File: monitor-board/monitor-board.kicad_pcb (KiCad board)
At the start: 2 copper layers, 55.9 x 53.3 mm, 26 parts, among them SW1 SW_IO12, SW2 SW_IO13, SW3 SW_IO14, SW4 SW_IO15, SW5 SW_IO32, SW6 SW_IO33, SW7 SW_IO34, SW8 SW_IO35, U1 ESP32-WROOM-32, U2 TLV75533PDBV

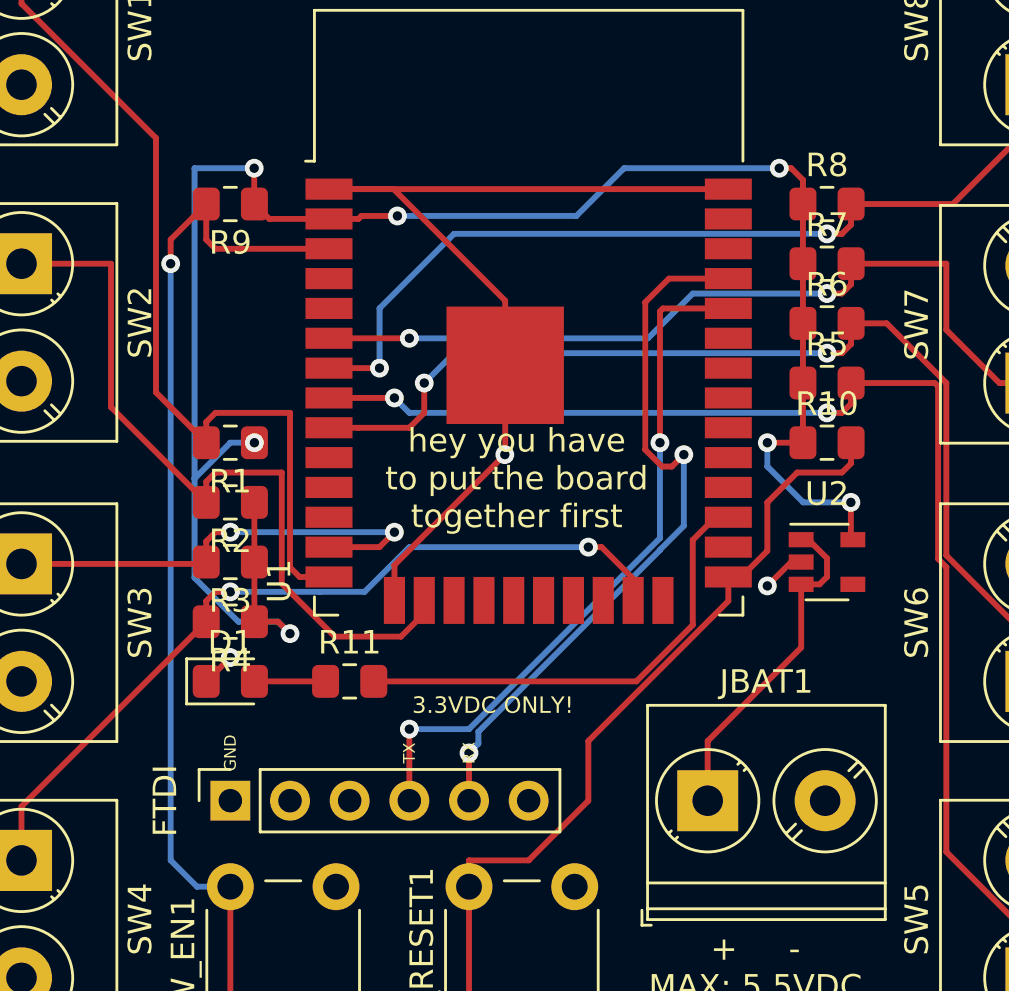
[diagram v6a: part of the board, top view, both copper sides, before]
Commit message: Update footprints of resistors and led to go with cheap parts
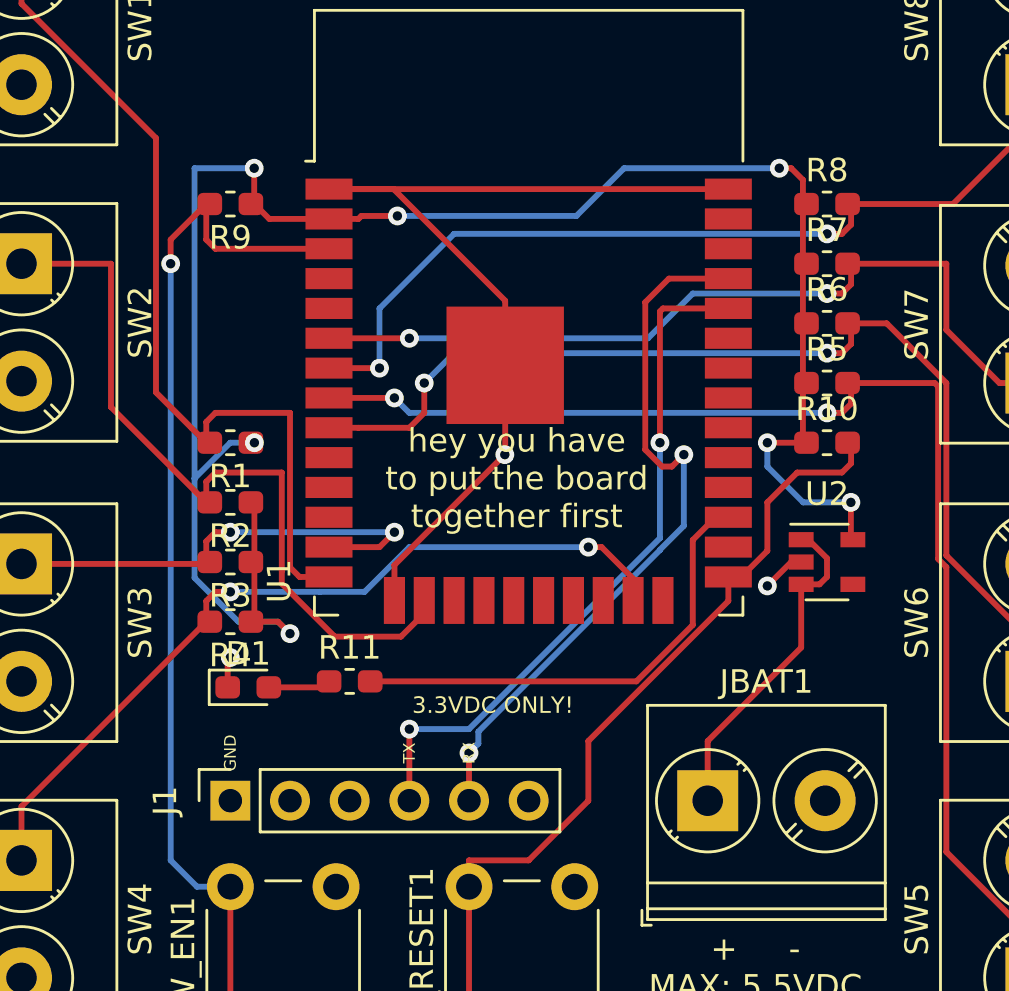
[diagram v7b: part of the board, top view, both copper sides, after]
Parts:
- D1: footprint LED_SMD:LED_0805_2012Metric_Pad1.15x1.40mm_HandSolder -> LED_SMD:LED_0603_1608Metric_Pad1.05x0.95mm_HandSolder
- R1, R10, R11, R2, R3, R4, R5, R6, R7, R8, R9: footprint Resistor_SMD:R_0805_2012Metric_Pad1.15x1.40mm_HandSolder -> Resistor_SMD:R_0603_1608Metric_Pad1.05x0.95mm_HandSolder
- moved D1 0.80 mm to (41.4, 61.2)
- renumbered FTDI to J1
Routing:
- net Net-(D1-Pad2): track 3.03 -> 2.52 mm

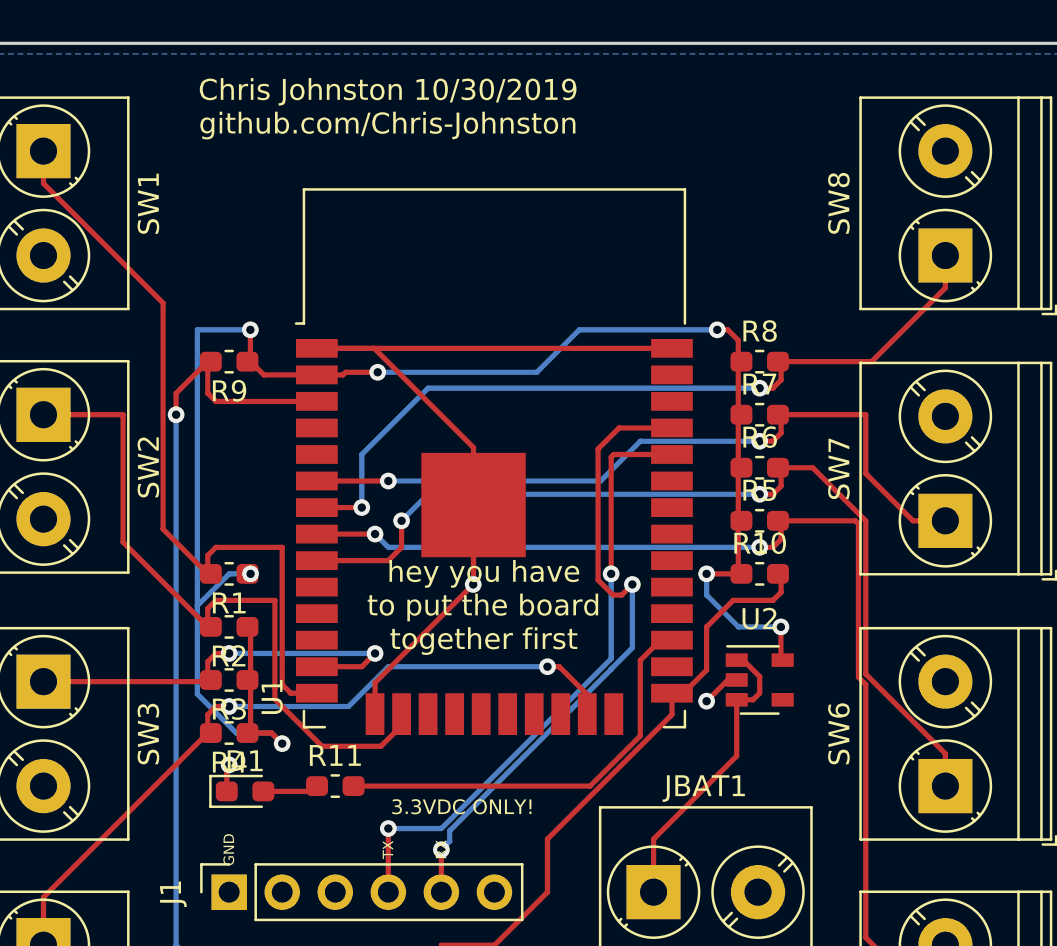
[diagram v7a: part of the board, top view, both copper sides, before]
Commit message: dont add crob image
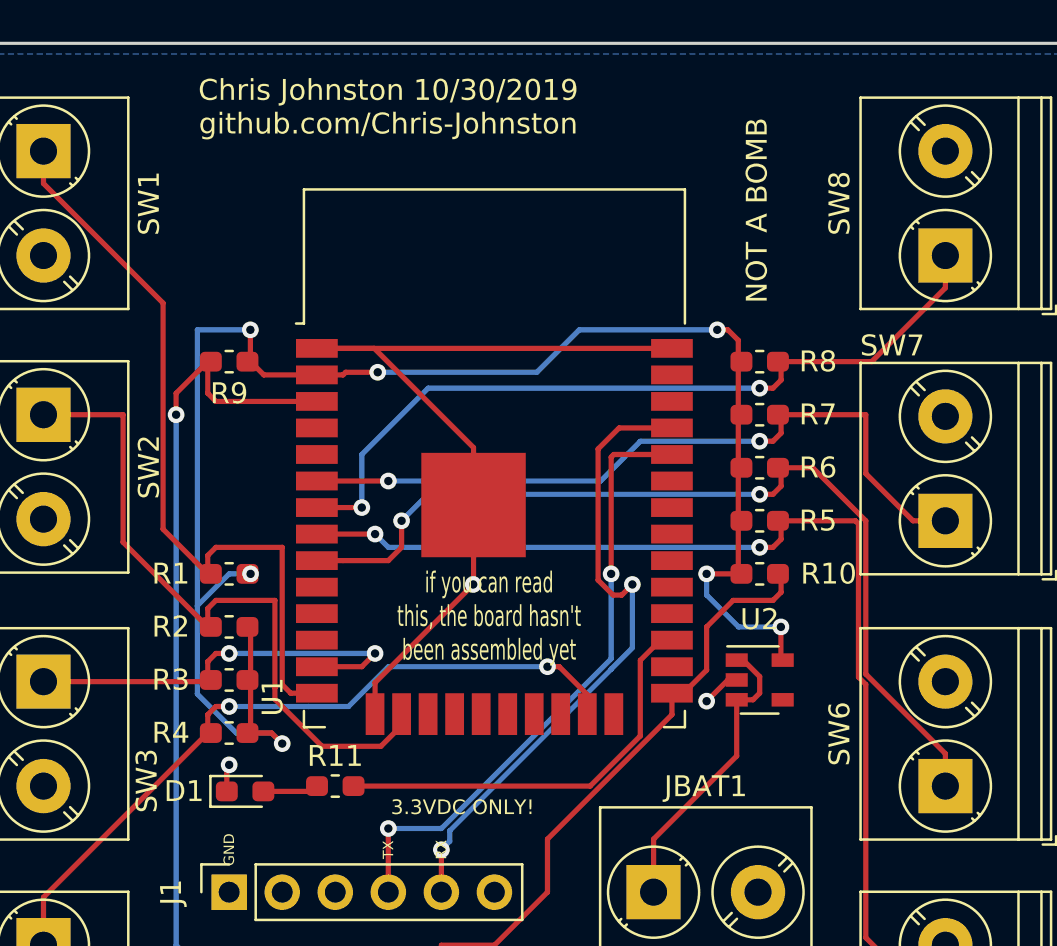
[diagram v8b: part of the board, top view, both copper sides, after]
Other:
- board text added: "FRONT TOWARD ENEMY"
- board text added: "NOT A BOMB"
- board text added: "if you can read this, the board hasn't been assembled yet"
- board text removed: "hey you have to put the board together first"
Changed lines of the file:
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@@
   (general
     (thickness 1.6)
-    (drawings 12)
+    (drawings 14)
     (tracks 225)
     (zones 0)
@@
   (page A4)
   (layers
-    (0 F.Cu signal)
-    (31 B.Cu signal)
-    (33 F.Adhes user)
-    (35 F.Paste user)
+    (0 F.Cu signal hide)
+    (31 B.Cu signal hide)
+    (33 F.Adhes user hide)
+    (35 F.Paste user hide)
+    (36 B.SilkS user)
     (37 F.SilkS user)
     (39 F.Mask user)
-    (40 Dwgs.User user)
-    (41 Cmts.User user)
-    (42 Eco1.User user)
-    (43 Eco2.User user)
+    (40 Dwgs.User user hide)
+    (41 Cmts.User user hide)
+    (42 Eco1.User user hide)
+    (43 Eco2.User user hide)
     (44 Edge.Cuts user)
-    (45 Margin user)
-    (46 B.CrtYd user)
-    (47 F.CrtYd user)
-    (49 F.Fab user)
+    (45 Margin user hide)
+    (46 B.CrtYd user hide)
+    (47 F.CrtYd user hide)
+    (49 F.Fab user hide)
   )
   (setup
@@
     (descr "Terminal Block Phoenix PT-1,5-2-5.0-H, 2 pins, pitch 5mm, size 10x9mm^2, drill diamater 1.3mm, pad diameter 2.6mm, see http://www.mouser.com/ds/2/324/ItemDetail_1935161-922578.pdf, script-generated using https://github.com/pointhi/kicad-footprint-generator/scripts/TerminalBlock_Phoenix")
     (tags "THT Terminal Block Phoenix PT-1,5-2-5.0-H pitch 5mm size 10x9mm^2 drill 1.3mm pad 2.6mm")
-    (fp_text reference SW3 (at 2.5 -5.06 90) (layer F.SilkS)
+    (fp_text reference SW3 (at 4.746 -4.953 90) (layer F.SilkS)
       (effects (font (size 1 1) (thickness 0.15)))
     )
@@
     (descr "Terminal Block Phoenix PT-1,5-2-5.0-H, 2 pins, pitch 5mm, size 10x9mm^2, drill diamater 1.3mm, pad diameter 2.6mm, see http://www.mouser.com/ds/2/324/ItemDetail_1935161-922578.pdf, script-generated using https://github.com/pointhi/kicad-footprint-generator/scripts/TerminalBlock_Phoenix")
     (tags "THT Terminal Block Phoenix PT-1,5-2-5.0-H pitch 5mm size 10x9mm^2 drill 1.3mm pad 2.6mm")
-    (fp_text reference SW7 (at 2.5 -5.06 90) (layer F.SilkS)
+    (fp_text reference SW7 (at 8.382 -2.54 180) (layer F.SilkS)
       (effects (font (size 1 1) (thickness 0.15)))
     )
@@
     (tags "LED handsolder")
     (attr smd)
-    (fp_text reference D1 (at 0 -1.43) (layer F.SilkS)
+    (fp_text reference D1 (at -2.921 0) (layer F.SilkS)
       (effects (font (size 1 1) (thickness 0.15)))
     )
@@
     (tags "resistor handsolder")
     (attr smd)
-    (fp_text reference R1 (at 0 -1.43) (layer F.SilkS)
+    (fp_text reference R1 (at 2.794 0) (layer F.SilkS)
       (effects (font (size 1 1) (thickness 0.15)))
     )
@@
     (tags "resistor handsolder")
     (attr smd)
-    (fp_text reference R2 (at 0 -1.43) (layer F.SilkS)
+    (fp_text reference R2 (at 2.794 0) (layer F.SilkS)
       (effects (font (size 1 1) (thickness 0.15)))
     )
@@
     (tags "resistor handsolder")
     (attr smd)
-    (fp_text reference R3 (at 0 -1.43) (layer F.SilkS)
+    (fp_text reference R3 (at 2.794 0) (layer F.SilkS)
       (effects (font (size 1 1) (thickness 0.15)))
     )
@@
     (tags "resistor handsolder")
     (attr smd)
-    (fp_text reference R4 (at 0 -1.43) (layer F.SilkS)
+    (fp_text reference R4 (at 2.794 0) (layer F.SilkS)
       (effects (font (size 1 1) (thickness 0.15)))
     )
@@
     (tags "resistor handsolder")
     (attr smd)
-    (fp_text reference R5 (at 0 -1.43) (layer F.SilkS)
+    (fp_text reference R5 (at 2.794 0) (layer F.SilkS)
       (effects (font (size 1 1) (thickness 0.15)))
     )
@@
     (tags "resistor handsolder")
     (attr smd)
-    (fp_text reference R6 (at 0 -1.43) (layer F.SilkS)
+    (fp_text reference R6 (at 2.794 0) (layer F.SilkS)
       (effects (font (size 1 1) (thickness 0.15)))
     )
@@
     (tags "resistor handsolder")
     (attr smd)
-    (fp_text reference R7 (at 0 -1.43) (layer F.SilkS)
+    (fp_text reference R7 (at 2.794 0) (layer F.SilkS)
       (effects (font (size 1 1) (thickness 0.15)))
     )
@@
     (tags "resistor handsolder")
     (attr smd)
-    (fp_text reference R8 (at 0 -1.43) (layer F.SilkS)
+    (fp_text reference R8 (at 2.794 0) (layer F.SilkS)
       (effects (font (size 1 1) (thickness 0.15)))
     )
@@
     (tags "resistor handsolder")
     (attr smd)
-    (fp_text reference R9 (at 0 -1.43) (layer F.SilkS)
+    (fp_text reference R9 (at 0 -1.524) (layer F.SilkS)
       (effects (font (size 1 1) (thickness 0.15)))
     )
@@
     (tags "resistor handsolder")
     (attr smd)
-    (fp_text reference R10 (at 0 -1.43) (layer F.SilkS)
+    (fp_text reference R10 (at 3.302 0) (layer F.SilkS)
       (effects (font (size 1 1) (thickness 0.15)))
     )
@@
     )
   )
+  (gr_text "NOT A BOMB" (at 65.913 33.401 90) (layer F.SilkS)
+    (effects (font (size 1 1) (thickness 0.15)))
+  )
+  (gr_text "FRONT\nTOWARD ENEMY" (at 53.213 40.64) (layer B.SilkS)
+    (effects (font (size 1 1) (thickness 0.15)) (justify mirror))
+  )
   (gr_text "3.3VDC ONLY!" (at 51.816 61.976) (layer F.SilkS)
     (effects (font (size 0.7 0.7) (thickness 0.15)))
@@
     (effects (font (size 1 1) (thickness 0.15)))
   )
-  (gr_text "hey you have\nto put the board\ntogether first" (at 52.832 52.324) (layer F.SilkS)
-    (effects (font (size 1 1) (thickness 0.15)))
+  (gr_text "if you can read\nthis, the board hasn't\nbeen assembled yet" (at 53.086 52.832) (layer F.SilkS)
+    (effects (font (size 1 0.6) (thickness 0.15)))
   )
   (gr_text "Warranty void if sticker removed" (at 66.548 77.216) (layer F.SilkS)
